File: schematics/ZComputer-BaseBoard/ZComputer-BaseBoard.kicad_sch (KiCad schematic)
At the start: 23 parts, among them J1 Board to board connector, J10 Board to board connector, J11 Board to board connector, J2 Board to board connector, J3 Board to board connector, J4 Board to board connector, J5 Board to board connector, J6 Board to board connector, J7 Board to board connector, J8 Board to board connector, J9 Conn_micro_USB_board, SW1 RESET_SW

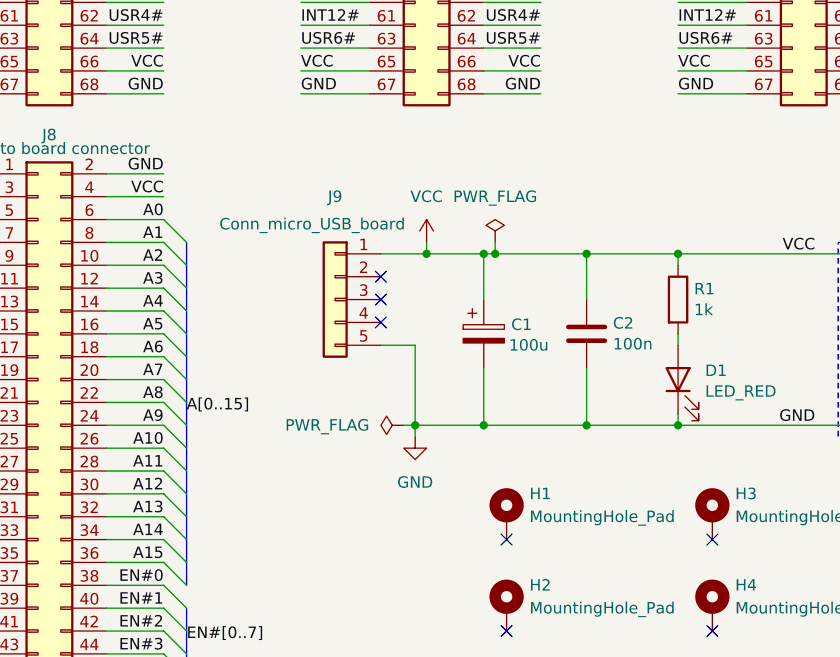
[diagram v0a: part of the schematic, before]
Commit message: Add power switch on the base board
Signed-off-by: Maxime Chretien <mchretien@linuxmail.org>
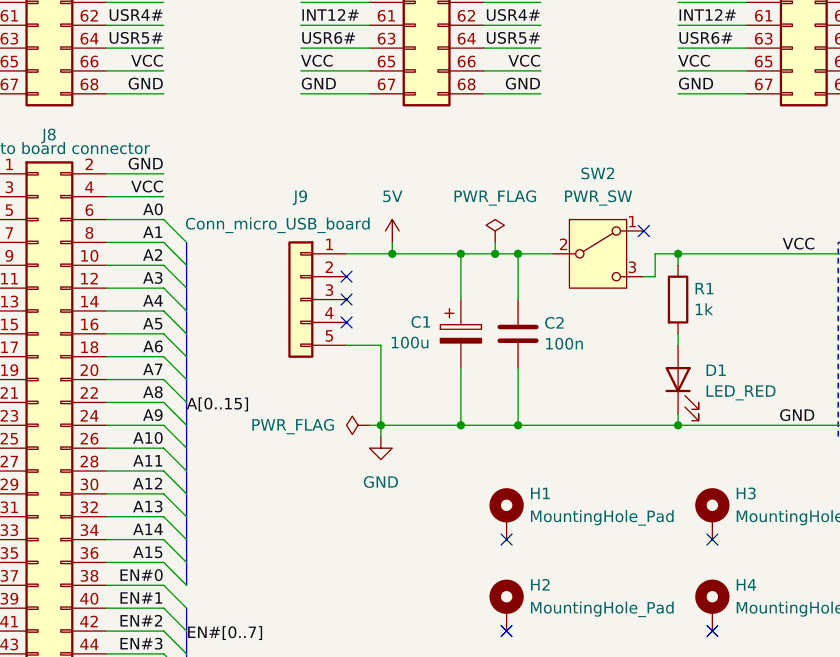
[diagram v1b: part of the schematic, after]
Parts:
- added SW2: PWR_SW, Button_Switch_THT:SW_Slide_SPDT_Angled_CK_OS102011MA1Q, symbol Switch:SW_SPDT
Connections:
- net VCC: now also SW2.3 (C); no longer C1.1, C2.1, J9.1 (Pin_1)
- new net 5V: C1.1, C2.1, J9.1 (Pin_1), SW2.2 (B)
- no-connect marks 9 -> 10
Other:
- moved on the sheet: C1, C2, J9
